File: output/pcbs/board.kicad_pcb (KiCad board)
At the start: 2 copper layers, 169.9 x 163.3 mm, 89 parts

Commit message: changed the thumb cluster column names to be clear and prevent overlaps
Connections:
- net bottom_far renamed t_col2_far
- net bottom_near renamed t_col2_near
- net middle_far renamed t_col1_far
- net middle_near renamed t_col1_near
- net top_near renamed t_col0_near
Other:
- outline, holes or cut-outs redrawn

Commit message: auto-route the switch-diode routes
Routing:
- net ring_top: track 4.72 -> 15.0 mm
- net ring_num: track 4.72 -> 15.0 mm
- net ring_mod: track 4.72 -> 15.0 mm
- net ring_home: track 4.72 -> 15.0 mm
- net ring_bottom: track 4.72 -> 15.0 mm
- net pinky_top: track 4.72 -> 15.0 mm
- net pinky_num: track 4.72 -> 15.0 mm
- net pinky_mod: track 4.72 -> 15.0 mm
- net pinky_home: track 4.72 -> 15.0 mm
- net pinky_bottom: track 4.72 -> 15.0 mm
- net outer_top: track 4.72 -> 15.0 mm
- net outer_num: track 4.72 -> 15.0 mm
- net outer_mod: track 4.72 -> 15.0 mm
- net outer_home: track 4.72 -> 15.0 mm
- net outer_bottom: track 4.72 -> 15.0 mm
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
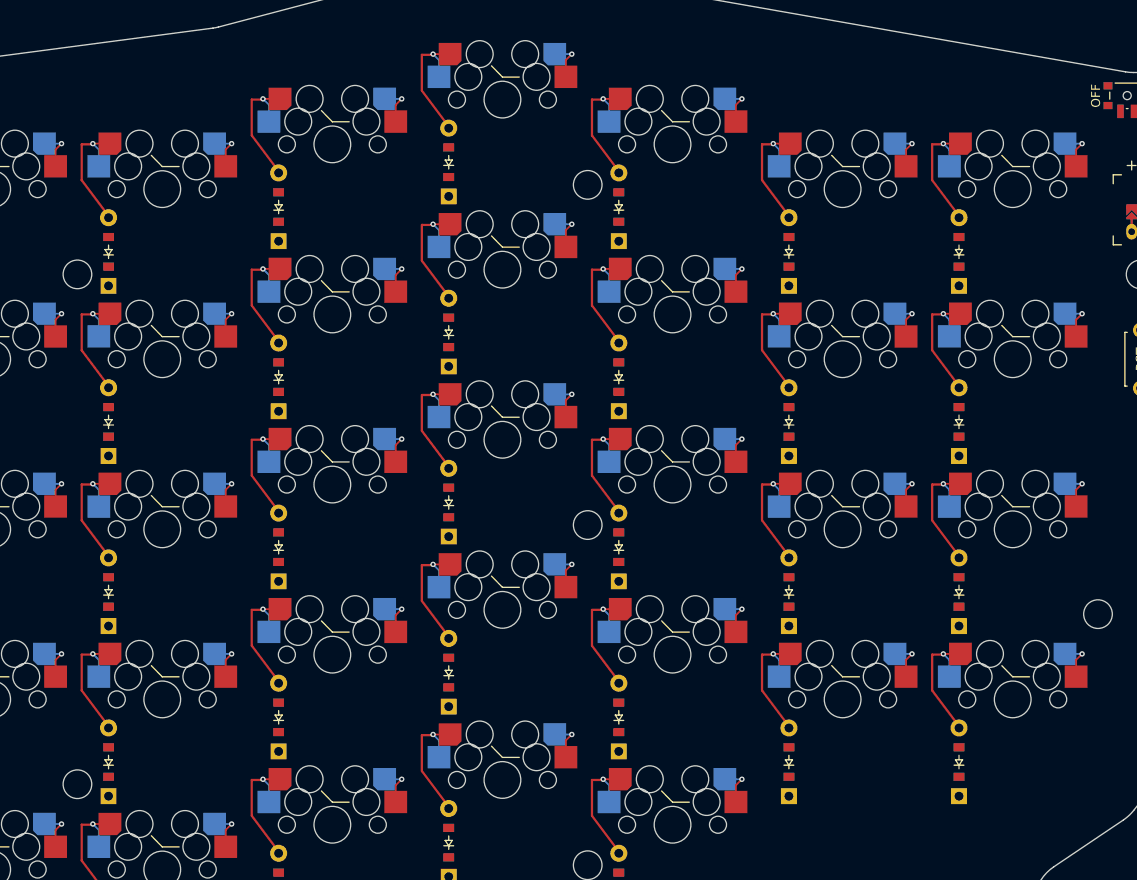
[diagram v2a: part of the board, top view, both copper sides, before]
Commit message: Route column nets
renamed inner_mod column to innermod to make regex matching simpler
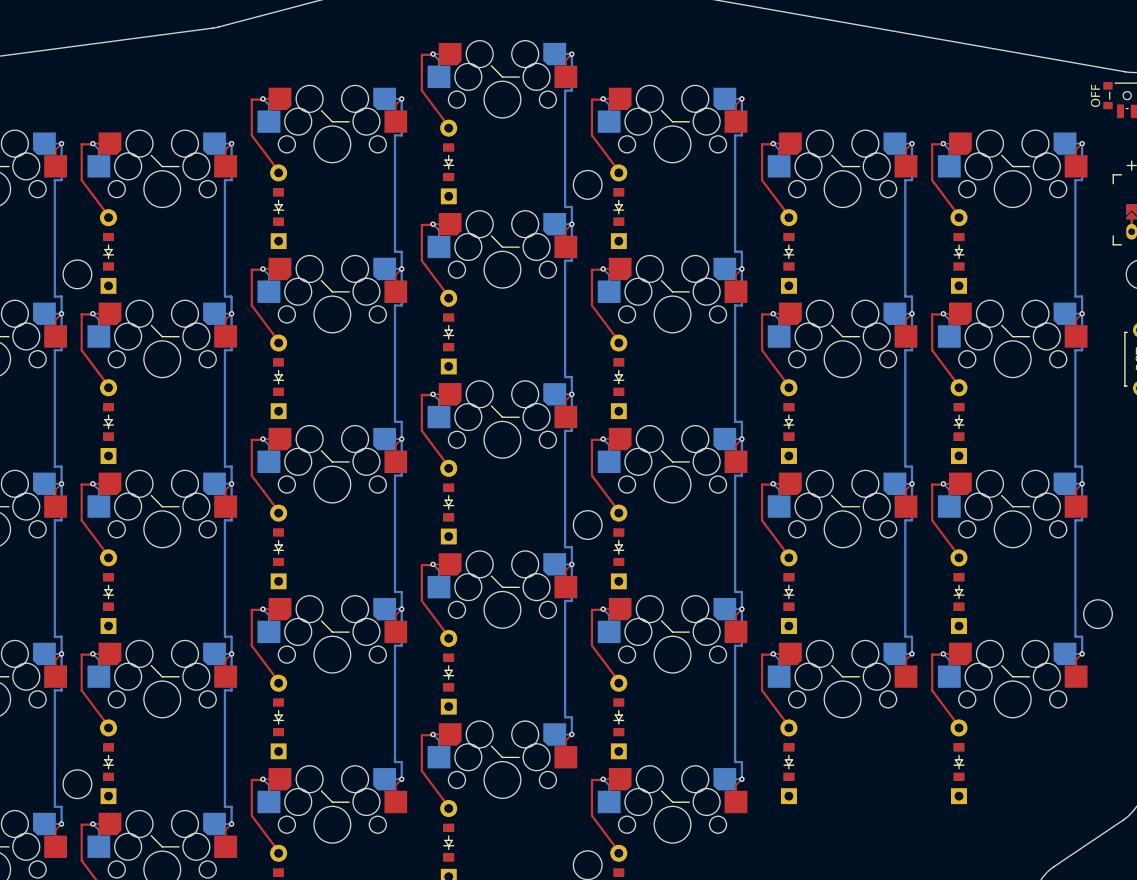
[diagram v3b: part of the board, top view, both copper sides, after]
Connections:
- net inner_mod_bottom renamed innermod_bottom
- net inner_mod_home renamed innermod_home
- net inner_mod_num renamed innermod_num
- net inner_mod_top renamed innermod_top
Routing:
- net (no net): track 345.4 -> 878.4 mm
